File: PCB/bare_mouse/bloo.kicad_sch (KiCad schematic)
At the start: 99 parts, among them J1 Serial Debug Header, J10 Conn_01x06_Female, J4 Conn_ARM_JTAG_SWD_10, J5 SWD Header, M3 M1_Conn_Alt, M4 M2_Conn_Alt, Q0 TEFT4300, Q1 TEFT4300, Q10 Q_NMOS_GSD, Q11 Q_NMOS_GSD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

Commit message: Updated BOM with changes associated with motor driver and removal of 100k resistors
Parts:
- removed M3: M1_Conn_Alt, MM_Library:Motor Headers, symbol Connector:Conn_01x06_Female
- removed M4: M2_Conn_Alt, MM_Library:Motor Headers, symbol Connector:Conn_01x06_Female
- removed R10, R9: 100K, Resistor_SMD:R_1206_3216Metric_Pad1.30x1.75mm_HandSolder, symbol Device:R
- removed U2: L293D, Package_DIP:DIP-16_W7.62mm, symbol Driver_Motor:L293D
- added C5: 0.1uF, Capacitor_SMD:C_1206_3216Metric_Pad1.33x1.80mm_HandSolder, symbol Device:C
- added C7: 10uF, Capacitor_SMD:C_1206_3216Metric_Pad1.33x1.80mm_HandSolder, symbol Device:C
- added M1: M1_Conn_Alt, MM_Library:Motor Headers, symbol Connector:Conn_01x06_Female
- added M2: M2_Conn_Alt, MM_Library:Motor Headers, symbol Connector:Conn_01x06_Female
- added U2: TB6612FNG, Package_SO:SSOP-24_5.3x8.2mm_P0.65mm, symbol Driver_Motor:TB6612FNG
- BZ1: footprint Buzzer_Beeper:Buzzer_12x9.5RM7.6 -> custom_foot:buzzer
- C3: value 0.1uF -> 10uF
- C4: value 1uF -> 0.1uF
- R18: value R -> 0
- R22: value R -> 20K
- R23: value R -> 10K
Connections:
- net +3V3: now also M1.3 (Pin_3), M2.3 (Pin_3)
- net +5V: now also C5.1, C7.1, U2.19 (STBY), U2.20 (VCC); no longer C3.1
- net GND: now also C5.2, C7.2, M1.6 (Pin_6), M2.6 (Pin_6), U2.10 (PGND2), U2.18 (GND), U2.3 (PGND1), U2.4 (PGND1), U2.9 (PGND2)
- net M1_BACK: now also U2.22 (AIN2)
- net M1_ENC_A: now also M2.4 (Pin_4)
- net M1_ENC_B: now also M2.5 (Pin_5)
- net M1_FWD: now also U2.21 (AIN1)
- net M1_OUT_1: now also M2.1 (Pin_1), U2.1 (AO1), U2.2 (AO1)
- net M1_OUT_2: now also M2.2 (Pin_2), U2.5 (AO2), U2.6 (AO2)
- net M1_SPD: now also U2.23 (PWMA)
- net M2_BACK: now also U2.16 (BIN2)
- net M2_ENC_A: now also M1.4 (Pin_4)
- net M2_ENC_B: now also M1.5 (Pin_5)
- net M2_FWD: now also U2.17 (BIN1)
- net M2_OUT_1: now also M1.1 (Pin_1), U2.11 (BO1), U2.12 (BO1)
- net M2_OUT_2: now also M1.2 (Pin_2), U2.7 (BO2), U2.8 (BO2)
- net M2_SPD: now also U2.15 (PWMB)
- net VCC: now also C3.1, U2.13 (VM2), U2.14 (VM3), U2.24 (VM1)

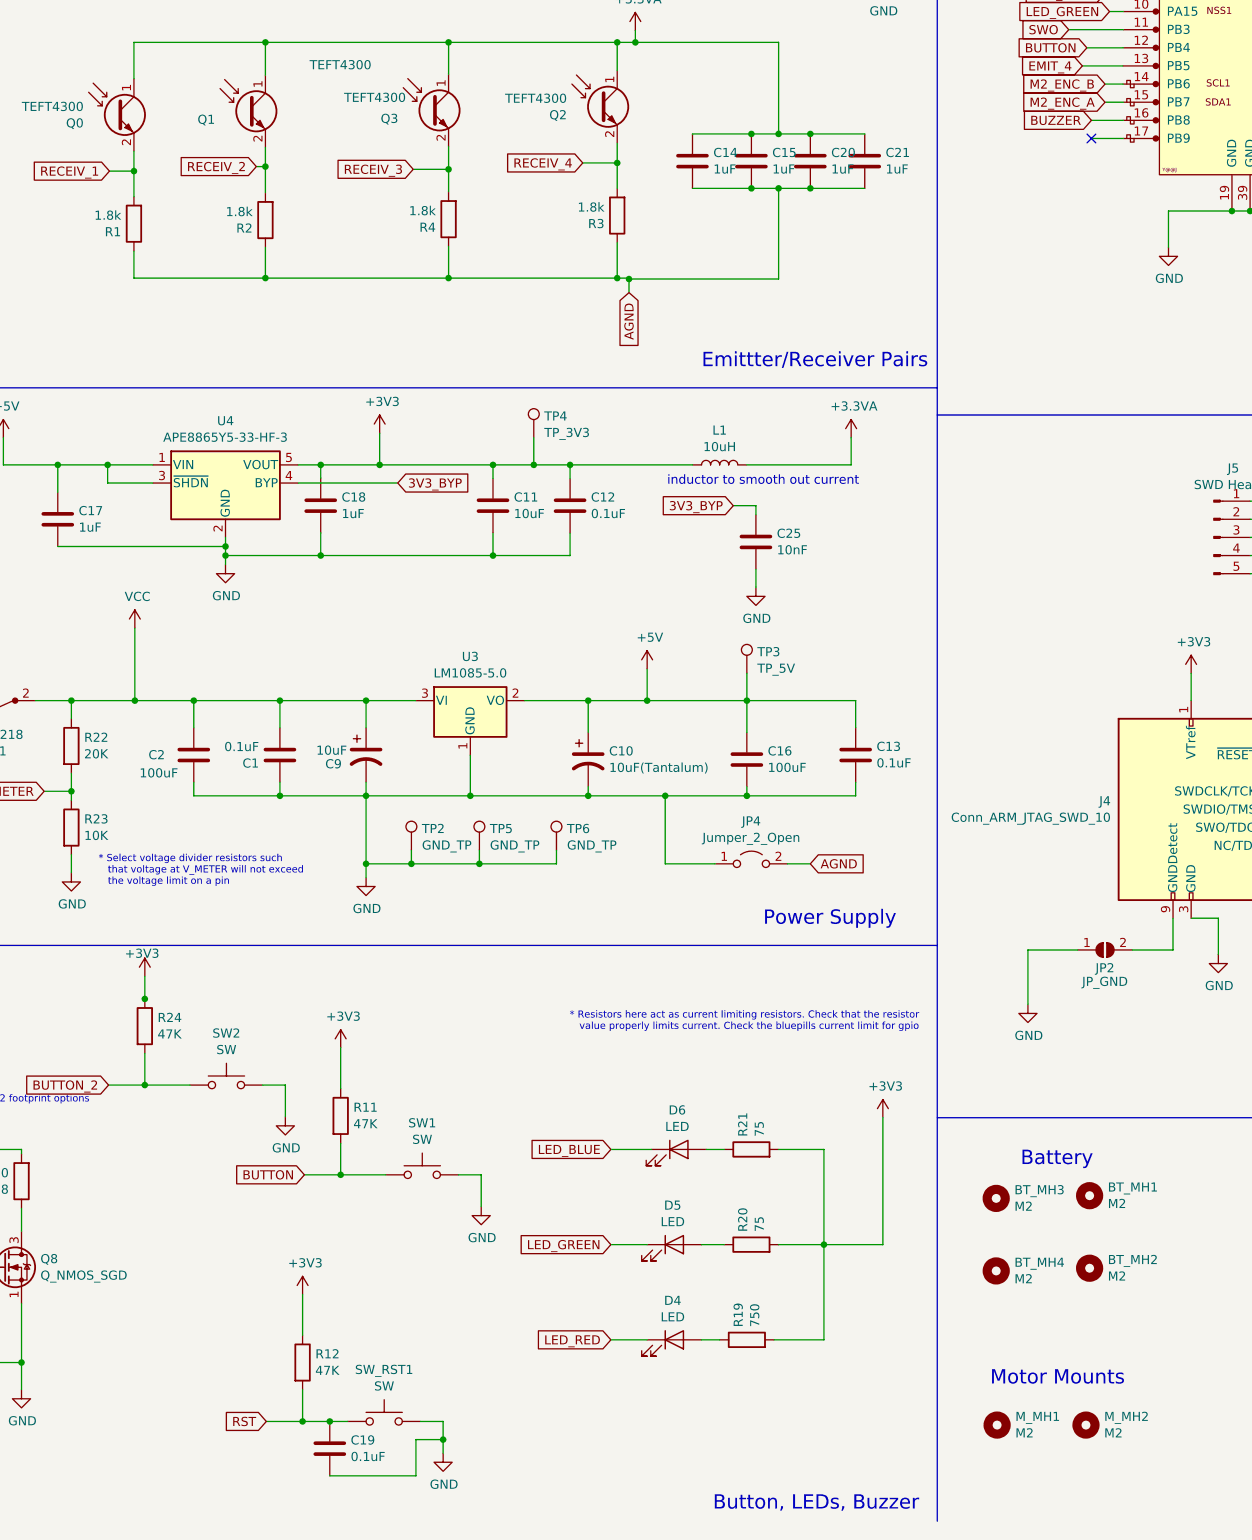
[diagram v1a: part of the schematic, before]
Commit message: Added button, updated BOM
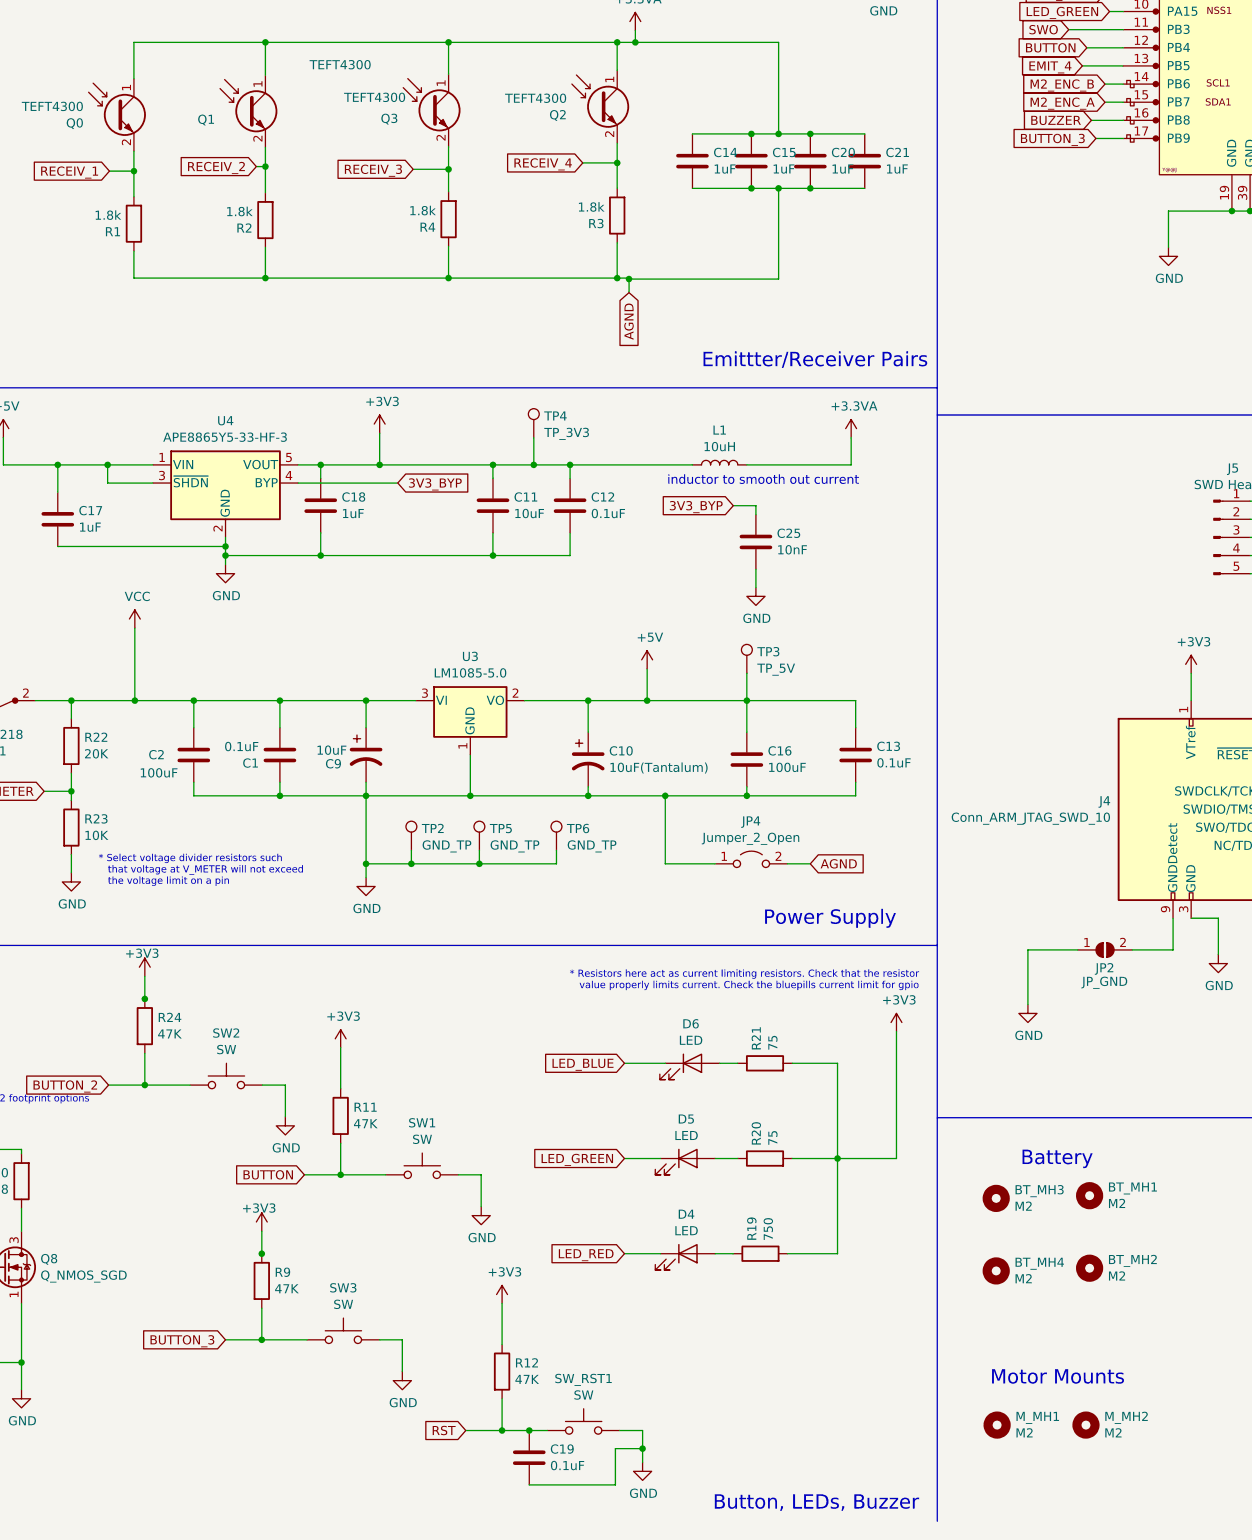
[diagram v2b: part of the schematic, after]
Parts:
- added R9: 47K, Resistor_SMD:R_1206_3216Metric_Pad1.30x1.75mm_HandSolder, symbol Device:R
- added SW3: SW, Button_Switch_SMD:SW_SPST_REED_CT05-XXXX-G1, symbol Switch:SW_Push
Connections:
- net +3V3: now also R9.1
- net GND: now also SW3.2
- net BUTTON_3: now reaches U1.17 (PB9)
- net BUTTON_3: now also R9.2, SW3.1
- no-connect marks 10 -> 9
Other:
- moved on the sheet: C19, D4, D5, D6, R12, R19, R20, R21, SW_RST1

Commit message: Current state
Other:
- note added: "* Battery mount holes not necessary, optional for teams who want to design battery mounts"
- note added: "Battery Protection"
- note removed: "* Not sure 100K’s are needed"
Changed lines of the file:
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@@
+    (effects (font (size 2.0066 2.0066)) (justify right bottom))
+  )
+  (text "Battery Protection\n" (at 406.4 182.88 0)
     (effects (font (size 2.0066 2.0066)) (justify right bottom))
   )
@@
     (effects (font (size 0.9906 0.9906)) (justify right bottom))
   )
+  (text "* Battery mount holes not necessary, optional \nfor teams who want to design battery mounts"
+    (at 210.82 256.54 0)
+    (effects (font (size 0.9906 0.9906)) (justify right bottom))
+  )
   (text "Motor Driver" (at 388.62 111.125 0)
     (effects (font (size 2.0066 2.0066)) (justify left bottom))
   )
-  (text "* Not sure 100K’s are needed" (at 265.43 210.82 0)
-    (effects (font (size 0.9906 0.9906)) (justify right bottom))
-  )
   (text "Emittter/Receiver Pairs" (at 171.45 123.19 0)

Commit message: Added power ORing schematic. Updated BOM and added footprints/symbols
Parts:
- added J2: SWD Header, Connector_PinHeader_2.54mm:PinHeader_1x05_P2.54mm_Vertical, symbol Connector:Conn_01x05_Male
- added MOS1: SSM3K335R_LF, custom_foot:SOT-23F_TOS, symbol SSM3K3335R:SSM3K335R_LF
- added U5: LM66100DCKR, custom_foot:DCK6_TEX, symbol DCK6_TEX:LM66100DCKR
- added U6: LM66100DCKR, DCK6_TEX, symbol DCK6_TEX:LM66100DCKR
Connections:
- net +3V3: now also U5.6 (VOUT)
- net +5V: now also MOS1.1, U6.6 (VOUT); no longer C10.1, C13.1, C16.1, TP3.1, U3.2 (VO)
- net GND: now also J2.4 (Pin_4), U5.2 (GND), U5.5 (ST), U6.2 (GND), U6.5 (ST)
- net RST: now also J2.5 (Pin_5)
- net SWDCLK: now also J2.3 (Pin_3)
- net SWDIO: now also J2.2 (Pin_2)
- net VCC: now also MOS1.3; no longer C1.2, C2.1, C9.1, R22.1, S1.2, U3.3 (VI)
- new net +3V3_NET: J2.1 (Pin_1), U5.1 (VIN), U6.3 (*CE)
- new net +5V_NET: C10.1, C13.1, C16.1, TP3.1, U3.2 (VO), U5.3 (*CE), U6.1 (VIN)
- new net BATT_NET: C1.2, C2.1, C9.1, MOS1.2, R22.1, S1.2, U3.3 (VI)
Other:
- note added: "* Allows VCC to pass through if +5V passes through the ideal diode"
- note added: "* Top is ideal diode for STLINK 3V3 Bott is ideal diode for batt 5V"
- note added: "Power ORing"
- note removed: "Battery Protection"
- moved on the sheet: J4, J5, JP1, JP2, JP3
